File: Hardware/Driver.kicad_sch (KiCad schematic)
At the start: 12 parts, among them J1 Motor, U1 MP6540

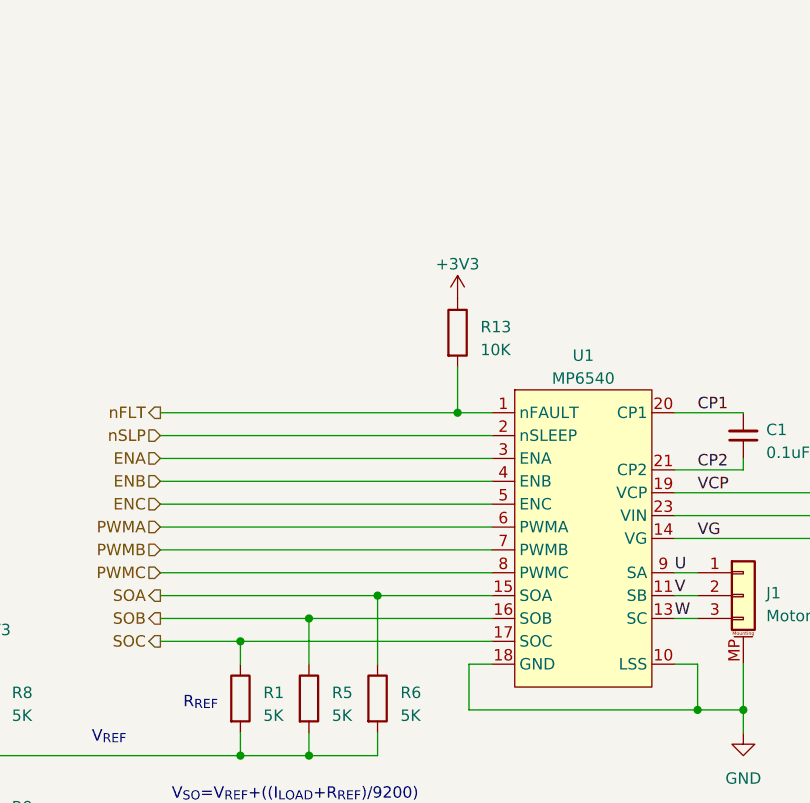
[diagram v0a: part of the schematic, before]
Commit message: 完成原理图设计，完成初步布局布线
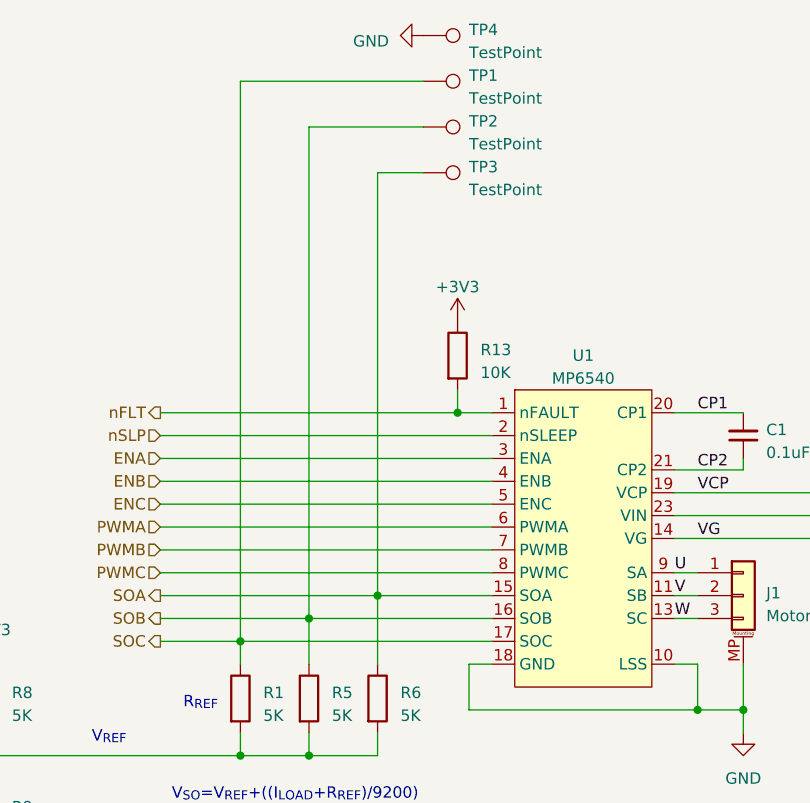
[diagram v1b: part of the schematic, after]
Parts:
- added TP1, TP2, TP3, TP4: TestPoint, TestPoint:TestPoint_Pad_D1.0mm, symbol Connector:TestPoint
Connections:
- net GND: now also TP4.1
- net SOA: now also TP3.1
- net SOB: now also TP2.1
- net SOC: now also TP1.1
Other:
- moved on the sheet: R13
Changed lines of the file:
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@@
+    (stroke (width 0) (type default))
+  )
+  (wire (pts (xy 113.03 40.64) (xy 113.03 102.87))
     (stroke (width 0) (type default))
   )
@@
     (stroke (width 0) (type default))
   )
+  (wire (pts (xy 133.35 40.64) (xy 113.03 40.64))
+    (stroke (width 0) (type default))
+  )
   (wire (pts (xy 113.03 102.87) (xy 140.97 102.87))
     (stroke (width 0) (type default))
@@
     (stroke (width 0) (type default))
   )
+  (wire (pts (xy 133.35 50.8) (xy 128.27 50.8))
+    (stroke (width 0) (type default))
+  )
   (wire (pts (xy 161.29 86.36) (xy 177.8 86.36))
     (stroke (width 0) (type default))
@@
     (stroke (width 0) (type default))
   )
+  (wire (pts (xy 128.27 50.8) (xy 128.27 97.79))
+    (stroke (width 0) (type default))
+  )
   (wire (pts (xy 104.14 77.47) (xy 137.16 77.47))
     (stroke (width 0) (type default))
@@
     (stroke (width 0) (type default))
   )
-  (wire (pts (xy 137.16 72.39) (xy 137.16 77.47))
+  (wire (pts (xy 137.16 74.93) (xy 137.16 77.47))
     (stroke (width 0) (type default))
   )
@@
     (stroke (width 0) (type default))
   )
+  (wire (pts (xy 133.35 45.72) (xy 120.65 45.72))
+    (stroke (width 0) (type default))
+  )
+  (wire (pts (xy 120.65 45.72) (xy 120.65 100.33))
+    (stroke (width 0) (type default))
+  )
   (wire (pts (xy 120.65 115.57) (xy 128.27 115.57))
     (stroke (width 0) (type default))
@@
     (effects (font (size 1.27 1.27)) (justify right))
   )
-  (symbol (lib_id "Device:R") (at 137.16 68.58 0) (unit 1)
-    (in_bom yes) (on_board yes) (dnp no) (fields_autoplaced)
-    (property "Reference" "R13" (at 139.7 67.945 0)
-      (effects (font (size 1.27 1.27)) (justify left))
-    )
-    (property "Value" "10K" (at 139.7 70.485 0)
-      (effects (font (size 1.27 1.27)) (justify left))
-    )
-    (property "Footprint" "myDevice:0603_R" (at 135.382 68.58 90)
-      (effects (font (size 1.27 1.27)) hide)
-    )
-    (property "Datasheet" "~" (at 137.16 68.58 0)
+  (symbol (lib_id "Device:R") (at 137.16 71.12 0) (unit 1)
+    (in_bom yes) (on_board yes) (dnp no) (fields_autoplaced)
+    (property "Reference" "R13" (at 139.7 70.485 0)
+      (effects (font (size 1.27 1.27)) (justify left))
+    )
+    (property "Value" "10K" (at 139.7 73.025 0)
+      (effects (font (size 1.27 1.27)) (justify left))
+    )
+    (property "Footprint" "myDevice:0603_R" (at 135.382 71.12 90)
+      (effects (font (size 1.27 1.27)) hide)
+    )
+    (property "Datasheet" "~" (at 137.16 71.12 0)
       (effects (font (size 1.27 1.27)) hide)
     )
@@
     )
   )
-  (symbol (lib_id "power:+3V3") (at 137.16 64.77 0) (unit 1)
-    (in_bom yes) (on_board yes) (dnp no) (fields_autoplaced)
-    (property "Reference" "#PWR047" (at 137.16 68.58 0)
-      (effects (font (size 1.27 1.27)) hide)
-    )
-    (property "Value" "+3V3" (at 137.16 60.96 0)
-      (effects (font (size 1.27 1.27)))
-    )
-    (property "Footprint" "" (at 137.16 64.77 0)
-      (effects (font (size 1.27 1.27)) hide)
-    )
-    (property "Datasheet" "" (at 137.16 64.77 0)
+  (symbol (lib_id "Connector:TestPoint") (at 133.35 35.56 270) (unit 1)
+    (in_bom yes) (on_board yes) (dnp no) (fields_autoplaced)
+    (property "Reference" "TP4" (at 138.43 34.925 90)
+      (effects (font (size 1.27 1.27)) (justify left))
+    )
+    (property "Value" "TestPoint" (at 138.43 37.465 90)
+      (effects (font (size 1.27 1.27)) (justify left))
+    )
+    (property "Footprint" "TestPoint:TestPoint_Pad_D1.0mm" (at 133.35 40.64 0)
+      (effects (font (size 1.27 1.27)) hide)
+    )
+    (property "Datasheet" "~" (at 133.35 40.64 0)
+      (effects (font (size 1.27 1.27)) hide)
+    )
+    (pin "1")
+    (instances
+      (project "cwFOC"
+        (path "/ff847474-9801-42c6-af12-b4b1b75aa0af/c3a6c5b4-78f3-47ea-a70d-c3f42438cf04"
+          (reference "TP4") (unit 1)
+        )
+      )
+    )
+  )
+  (symbol (lib_id "power:+3V3") (at 137.16 67.31 0) (unit 1)
+    (in_bom yes) (on_board yes) (dnp no) (fields_autoplaced)
+    (property "Reference" "#PWR047" (at 137.16 71.12 0)
+      (effects (font (size 1.27 1.27)) hide)
+    )
+    (property "Value" "+3V3" (at 137.16 63.5 0)
+      (effects (font (size 1.27 1.27)))
+    )
+    (property "Footprint" "" (at 137.16 67.31 0)
+      (effects (font (size 1.27 1.27)) hide)
+    )
+    (property "Datasheet" "" (at 137.16 67.31 0)
       (effects (font (size 1.27 1.27)) hide)
     )
@@
         (path "/ff847474-9801-42c6-af12-b4b1b75aa0af/c3a6c5b4-78f3-47ea-a70d-c3f42438cf04"
           (reference "#PWR047") (unit 1)
+        )
+      )
+    )
+  )
+  (symbol (lib_id "Connector:TestPoint") (at 133.35 40.64 270) (unit 1)
+    (in_bom yes) (on_board yes) (dnp no) (fields_autoplaced)
+    (property "Reference" "TP1" (at 138.43 40.005 90)
+      (effects (font (size 1.27 1.27)) (justify left))
+    )
+    (property "Value" "TestPoint" (at 138.43 42.545 90)
+      (effects (font (size 1.27 1.27)) (justify left))
+    )
+    (property "Footprint" "TestPoint:TestPoint_Pad_D1.0mm" (at 133.35 45.72 0)
+      (effects (font (size 1.27 1.27)) hide)
+    )
+    (property "Datasheet" "~" (at 133.35 45.72 0)
+      (effects (font (size 1.27 1.27)) hide)
+    )
+    (pin "1")
+    (instances
+      (project "cwFOC"
+        (path "/ff847474-9801-42c6-af12-b4b1b75aa0af/c3a6c5b4-78f3-47ea-a70d-c3f42438cf04"
+          (reference "TP1") (unit 1)
         )
       )
@@
         (path "/ff847474-9801-42c6-af12-b4b1b75aa0af/c3a6c5b4-78f3-47ea-a70d-c3f42438cf04"
           (reference "#PWR017") (unit 1)
+        )
+      )
+    )
+  )
+  (symbol (lib_id "power:GND") (at 133.35 35.56 270) (unit 1)
+    (in_bom yes) (on_board yes) (dnp no) (fields_autoplaced)
+    (property "Reference" "#PWR015" (at 127 35.56 0)
+      (effects (font (size 1.27 1.27)) hide)
+    )
+    (property "Value" "GND" (at 129.54 36.195 90)
+      (effects (font (size 1.27 1.27)) (justify right))
+    )
+    (property "Footprint" "" (at 133.35 35.56 0)
+      (effects (font (size 1.27 1.27)) hide)
+    )
+    (property "Datasheet" "" (at 133.35 35.56 0)
+      (effects (font (size 1.27 1.27)) hide)
+    )
+    (pin "1")
+    (instances
+      (project "cwFOC"
+        (path "/ff847474-9801-42c6-af12-b4b1b75aa0af/c3a6c5b4-78f3-47ea-a70d-c3f42438cf04"
+          (reference "#PWR015") (unit 1)
         )
       )
@@
     )
   )
+  (symbol (lib_id "Connector:TestPoint") (at 133.35 50.8 270) (unit 1)
+    (in_bom yes) (on_board yes) (dnp no) (fields_autoplaced)
+    (property "Reference" "TP3" (at 138.43 50.165 90)
+      (effects (font (size 1.27 1.27)) (justify left))
+    )
+    (property "Value" "TestPoint" (at 138.43 52.705 90)
+      (effects (font (size 1.27 1.27)) (justify left))
+    )
+    (property "Footprint" "TestPoint:TestPoint_Pad_D1.0mm" (at 133.35 55.88 0)
+      (effects (font (size 1.27 1.27)) hide)
+    )
+    (property "Datasheet" "~" (at 133.35 55.88 0)
+      (effects (font (size 1.27 1.27)) hide)
+    )
+    (pin "1")
+    (instances
+      (project "cwFOC"
+        (path "/ff847474-9801-42c6-af12-b4b1b75aa0af/c3a6c5b4-78f3-47ea-a70d-c3f42438cf04"
+          (reference "TP3") (unit 1)
+        )
+      )
+    )
+  )
   (symbol (lib_id "Device:C_Small") (at 168.91 80.01 180) (unit 1)
     (in_bom yes) (on_board yes) (dnp no) (fields_autoplaced)
@@
         )
       )
+    )
+  )
+  (symbol (lib_id "Connector:TestPoint") (at 133.35 45.72 270) (unit 1)
+    (in_bom yes) (on_board yes) (dnp no) (fields_autoplaced)
+    (property "Reference" "TP2" (at 138.43 45.085 90)
+      (effects (font (size 1.27 1.27)) (justify left))
+    )
+    (property "Value" "TestPoint" (at 138.43 47.625 90)
+      (effects (font (size 1.27 1.27)) (justify left))
+    )
+    (property "Footprint" "TestPoint:TestPoint_Pad_D1.0mm" (at 133.35 50.8 0)
+      (effects (font (size 1.27 1.27)) hide)
+    )
+    (property "Datasheet" "~" (at 133.35 50.8 0)
+      (effects (font (size 1.27 1.27)) hide)
+    )
+    (pin "1")
+    (instances
+      (project "cwFOC"
+        (path "/ff847474-9801-42c6-af12-b4b1b75aa0af/c3a6c5b4-78f3-47ea-a70d-c3f42438cf04"
+          (reference "TP2") (unit 1)
+        )
+      )

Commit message: 基本完成PCB设计
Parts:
- added R19: 0R, myDevice:0603_R, symbol Device:R
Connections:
- net GND: now also R19.1; no longer U1.10 (LSS), U1.12 (LSS)
- new net GNDPWR: R19.2, U1.10 (LSS), U1.12 (LSS)
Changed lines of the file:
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@@
   (junction (at 113.03 102.87) (diameter 0) (color 0 0 0 0)
   )
-  (junction (at 168.91 110.49) (diameter 0) (color 0 0 0 0)
-  )
   (junction (at 187.96 88.9) (diameter 0) (color 0 0 0 0)
   )
+  (junction (at 187.96 86.36) (diameter 0) (color 0 0 0 0)
+  )
+  (junction (at 138.43 110.49) (diameter 0) (color 0 0 0 0)
+  )
+  (junction (at 137.16 77.47) (diameter 0) (color 0 0 0 0)
+  )
+  (junction (at 85.09 115.57) (diameter 0) (color 0 0 0 0)
+  )
+  (junction (at 120.65 100.33) (diameter 0) (color 0 0 0 0)
+  )
   (junction (at 163.83 110.49) (diameter 0) (color 0 0 0 0)
   )
-  (junction (at 187.96 86.36) (diameter 0) (color 0 0 0 0)
-  )
-  (junction (at 137.16 77.47) (diameter 0) (color 0 0 0 0)
-  )
-  (junction (at 85.09 115.57) (diameter 0) (color 0 0 0 0)
-  )
-  (junction (at 120.65 100.33) (diameter 0) (color 0 0 0 0)
-  )
   (junction (at 187.96 99.06) (diameter 0) (color 0 0 0 0)
   )
@@
     (stroke (width 0) (type default))
   )
+  (wire (pts (xy 154.94 110.49) (xy 163.83 110.49))
+    (stroke (width 0) (type default))
+  )
   (wire (pts (xy 187.96 88.9) (xy 187.96 86.36))
     (stroke (width 0) (type default))
@@
     (stroke (width 0) (type default))
   )
+  (wire (pts (xy 163.83 110.49) (xy 163.83 113.03))
+    (stroke (width 0) (type default))
+  )
   (wire (pts (xy 113.03 102.87) (xy 140.97 102.87))
     (stroke (width 0) (type default))
@@
     (stroke (width 0) (type default))
   )
-  (wire (pts (xy 168.91 105.41) (xy 168.91 110.49))
-    (stroke (width 0) (type default))
-  )
   (wire (pts (xy 104.14 95.25) (xy 140.97 95.25))
     (stroke (width 0) (type default))
@@
     (stroke (width 0) (type default))
   )
+  (wire (pts (xy 138.43 110.49) (xy 147.32 110.49))
+    (stroke (width 0) (type default))
+  )
   (wire (pts (xy 104.14 77.47) (xy 137.16 77.47))
     (stroke (width 0) (type default))
@@
     (stroke (width 0) (type default))
   )
-  (wire (pts (xy 138.43 110.49) (xy 163.83 110.49))
-    (stroke (width 0) (type default))
-  )
   (wire (pts (xy 113.03 113.03) (xy 113.03 115.57))
     (stroke (width 0) (type default))
@@
     (stroke (width 0) (type default))
   )
-  (wire (pts (xy 163.83 110.49) (xy 168.91 110.49))
+  (wire (pts (xy 138.43 110.49) (xy 138.43 113.03))
     (stroke (width 0) (type default))
   )
@@
     (stroke (width 0) (type default))
   )
-  (wire (pts (xy 168.91 110.49) (xy 168.91 113.03))
+  (wire (pts (xy 168.91 105.41) (xy 168.91 113.03))
     (stroke (width 0) (type default))
   )
@@
     )
   )
+  (symbol (lib_id "power:GNDPWR") (at 163.83 113.03 0) (unit 1)
+    (in_bom yes) (on_board yes) (dnp no) (fields_autoplaced)
+    (property "Reference" "#PWR031" (at 163.83 118.11 0)
+      (effects (font (size 1.27 1.27)) hide)
+    )
+    (property "Value" "GNDPWR" (at 163.703 118.11 0)
+      (effects (font (size 1.27 1.27)))
+    )
+    (property "Footprint" "" (at 163.83 114.3 0)
+      (effects (font (size 1.27 1.27)) hide)
+    )
+    (property "Datasheet" "" (at 163.83 114.3 0)
+      (effects (font (size 1.27 1.27)) hide)
+    )
+    (pin "1")
+    (instances
+      (project "cwFOC"
+        (path "/ff847474-9801-42c6-af12-b4b1b75aa0af/50c76e34-9c76-4785-b3ad-3791bfa1e28e"
+          (reference "#PWR031") (unit 1)
+        )
+        (path "/ff847474-9801-42c6-af12-b4b1b75aa0af/c3a6c5b4-78f3-47ea-a70d-c3f42438cf04"
+          (reference "#PWR049") (unit 1)
+        )
+      )
+    )
+  )
   (symbol (lib_id "Device:R") (at 85.09 109.22 0) (unit 1)
     (in_bom yes) (on_board yes) (dnp no) (fields_autoplaced)
@@
     )
   )
+  (symbol (lib_id "power:GND") (at 138.43 113.03 0) (unit 1)
+    (in_bom yes) (on_board yes) (dnp no) (fields_autoplaced)
+    (property "Reference" "#PWR028" (at 138.43 119.38 0)
+      (effects (font (size 1.27 1.27)) hide)
+    )
+    (property "Value" "GND" (at 138.43 118.11 0)
+      (effects (font (size 1.27 1.27)))
+    )
+    (property "Footprint" "" (at 138.43 113.03 0)
+      (effects (font (size 1.27 1.27)) hide)
+    )
+    (property "Datasheet" "" (at 138.43 113.03 0)
+      (effects (font (size 1.27 1.27)) hide)
+    )
+    (pin "1")
+    (instances
+      (project "cwFOC"
+        (path "/ff847474-9801-42c6-af12-b4b1b75aa0af"
+          (reference "#PWR028") (unit 1)
+        )
+        (path "/ff847474-9801-42c6-af12-b4b1b75aa0af/c3a6c5b4-78f3-47ea-a70d-c3f42438cf04"
+          (reference "#PWR050") (unit 1)
+        )
+      )
+    )
+  )
   (symbol (lib_id "Device:C_Small") (at 180.34 86.36 270) (unit 1)
     (in_bom yes) (on_board yes) (dnp no) (fields_autoplaced)
@@
         )
       )
+    )
+  )
+  (symbol (lib_id "Device:R") (at 151.13 110.49 90) (unit 1)
+    (in_bom yes) (on_board yes) (dnp no) (fields_autoplaced)
+    (property "Reference" "R19" (at 151.13 114.3 90)
+      (effects (font (size 1.27 1.27)))
+    )
+    (property "Value" "0R" (at 151.13 116.84 90)
+      (effects (font (size 1.27 1.27)))
+    )
+    (property "Footprint" "myDevice:0603_R" (at 151.13 112.268 90)
+      (effects (font (size 1.27 1.27)) hide)
+    )
+    (property "Datasheet" "~" (at 151.13 110.49 0)
+      (effects (font (size 1.27 1.27)) hide)
+    )
+    (pin "1")
+    (pin "2")
+    (instances
+      (project "cwFOC"
+        (path "/ff847474-9801-42c6-af12-b4b1b75aa0af/c3a6c5b4-78f3-47ea-a70d-c3f42438cf04"
+          (reference "R19") (unit 1)
+        )
+      )

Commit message: 第一版硬件做好啦！(●'◡'●)
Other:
- company: (none) -> Akako Industry
- title: (none) -> cwFOC/Driver
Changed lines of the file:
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@@
 (kicad_sch (version 20230121) (generator eeschema)
   (paper "A4")
+  (title_block
+    (title "cwFOC/Driver")
+    (date "2023-03-19")
+    (rev "1.0")
+    (company "Akako Industry")
+    (comment 1 "赤紫绮")
+    (comment 2 "赤紫绮")
+    (comment 3 "赤紫绮")
+  )
   (junction (at 113.03 102.87) (diameter 0) (color 0 0 0 0)
   )

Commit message: 调整第二版原理图
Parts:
- added C13, C14, C15: 10pF, myDevice:0603_C, symbol Device:C
- added D2, D3, D4: SMAJ15CA, Diode_SMD:D_SMA, symbol Device:D_TVS
- added D5: SS54, Diode_SMD:D_SMB, symbol Device:D_Schottky
- added R20, R21, R22: 22R, myDevice:0603_R, symbol Device:R
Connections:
- net GND: now also C13.1, C14.1, C15.1
- net GNDPWR: now also D2.1 (A1), D3.1 (A1), D4.1 (A1)
- net SOA: now also C15.2, R20.1; no longer U1.15 (SOA)
- net SOB: now also C14.2, R21.1; no longer U1.16 (SOB)
- net SOC: now also C13.2, R22.1; no longer U1.17 (SOC)
- net U: now also D4.2 (A2)
- net V: now also D3.2 (A2)
- net VBUS: now also D5.2 (A); no longer C11.1, C5.1, U1.23 (VIN), U1.25 (VIN)
- net W: now also D2.2 (A2)
- new net: R21.2, U1.16 (SOB)
- new net: R22.2, U1.17 (SOC)
- new net: R20.2, U1.15 (SOA)
- new net VIN: C11.1, C5.1, D5.1 (K), U1.23 (VIN), U1.25 (VIN)
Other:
- moved on the sheet: C10, C11, C5, J1, R8, R9
